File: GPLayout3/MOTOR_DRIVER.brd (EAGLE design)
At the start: 129.7 x 96.6 mm, 95 parts, among them T1 2N2222, T2 2N2222, U7 ATMEGA328P_TQFP, Y1 16MHz

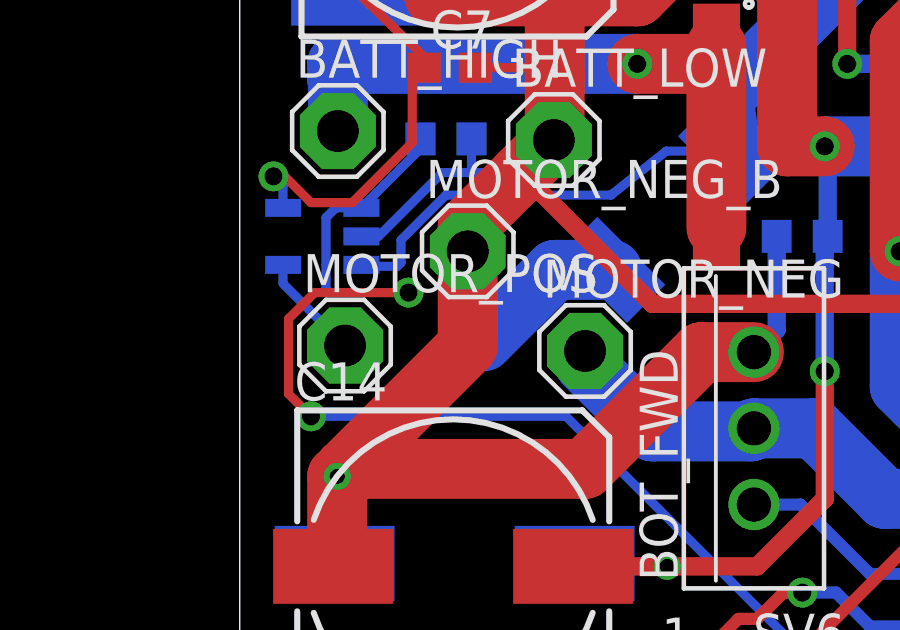
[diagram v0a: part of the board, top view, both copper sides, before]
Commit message: Fixed missing wire
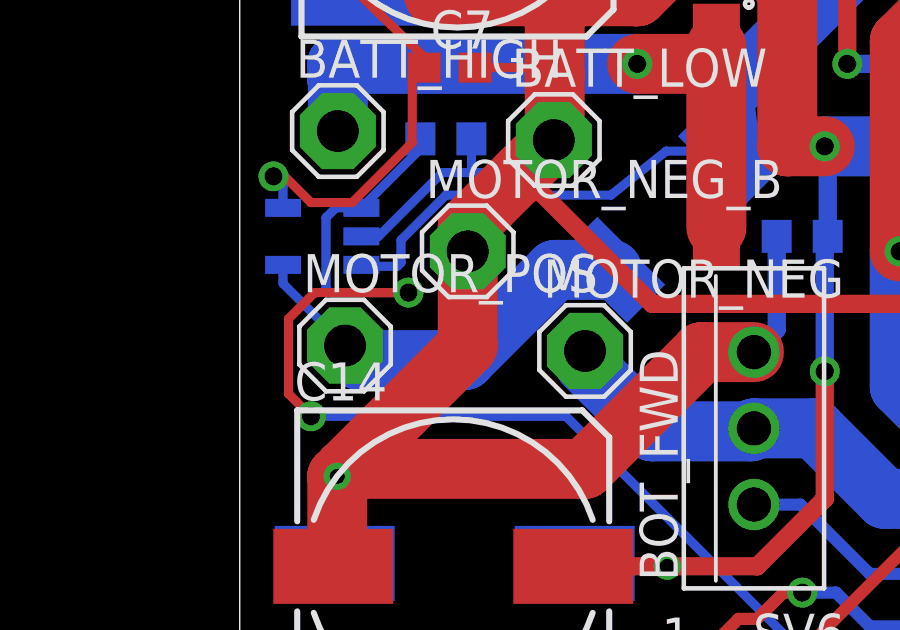
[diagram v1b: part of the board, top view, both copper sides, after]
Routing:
- net I_SENSE_LOW_TOP: track 9.02 -> 14.1 mm
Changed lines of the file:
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@@
 <wire x1="12.41464375" y1="67.38185" x2="10.50685" y2="67.38185" width="2" layer="16"/>
 <wire x1="3.51" y1="64.86" x2="3.65" y2="65" width="2" layer="16"/>
-<wire x1="10.50685" y1="67.38185" x2="8.125" y2="65" width="2" layer="16"/>
 <wire x1="1.444" y1="67.55" x2="1.444" y2="66.926" width="0.3048" layer="16"/>
 <wire x1="1.444" y1="66.926" x2="3.51" y2="64.86" width="0.3048" layer="16"/>
-<wire x1="3.65" y1="65" x2="8.125" y2="65" width="0" layer="19" extent="16-16"/>
+<wire x1="7.5" y1="64.375" x2="3.995" y2="64.375" width="2" layer="16"/>
+<wire x1="3.995" y1="64.375" x2="3.51" y2="64.86" width="2" layer="16"/>
+<wire x1="10.50685" y1="67.38185" x2="7.5" y2="64.375" width="2" layer="16"/>
 </signal>
 <signal name="I_SENSE_HI">

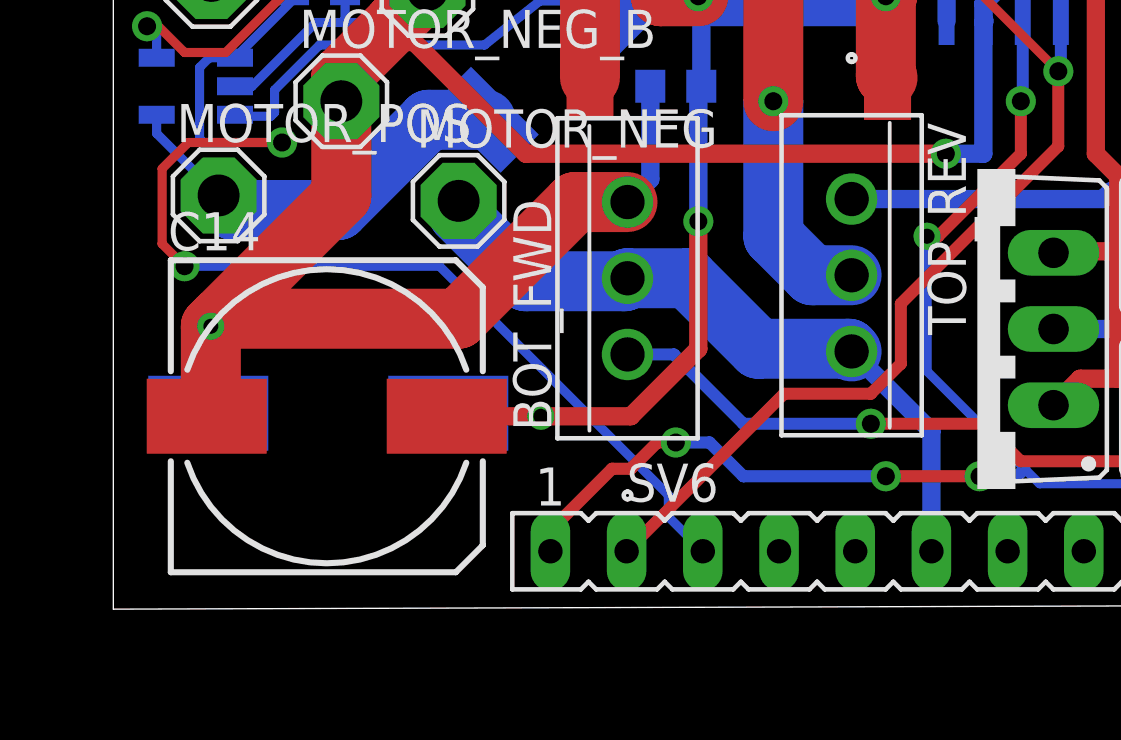
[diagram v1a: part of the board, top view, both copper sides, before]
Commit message: Fixed missing motor_high_top pin, now I_SENSE_LOW_TOP
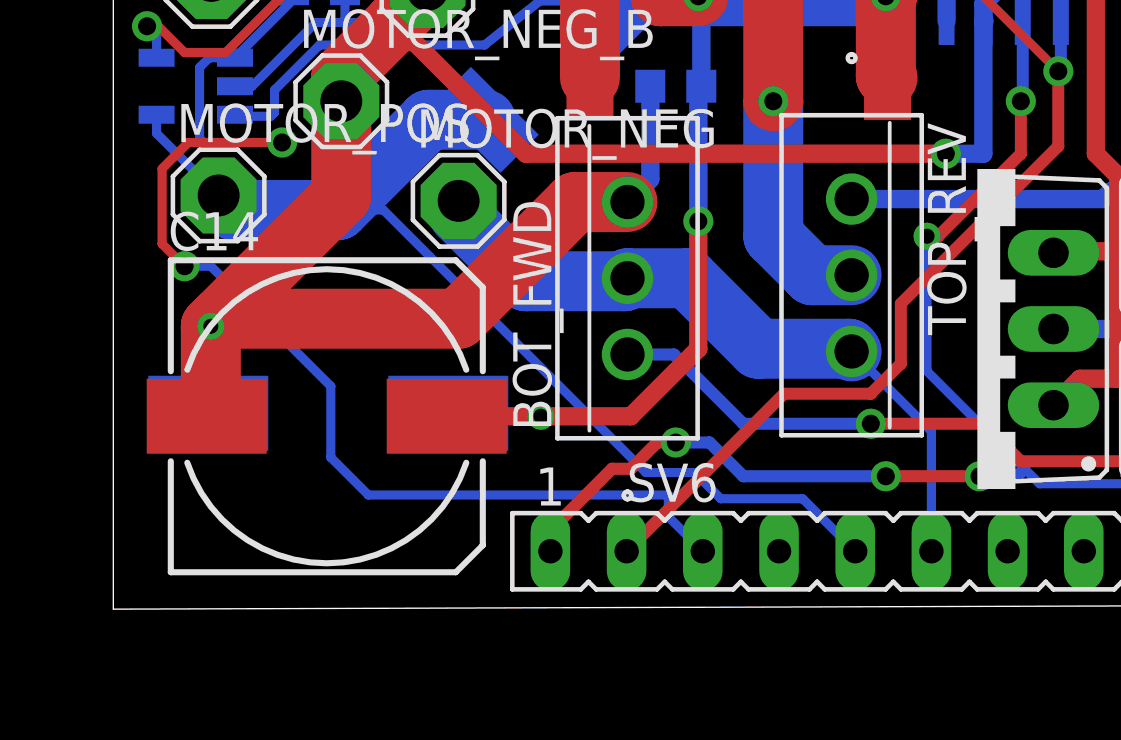
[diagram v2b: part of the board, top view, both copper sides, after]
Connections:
- removed net MOTOR_HIGH_TOP: SV6.5
- net I_SENSE_LOW_TOP: now also SV6.5
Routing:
- net I_SENSE_LOW_TOP: track 14.1 -> 36.0 mm
- net I_SENSE_TOP: track 39.2 -> 40.6 mm
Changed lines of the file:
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@@
 <wire x1="18.51" y1="23.49" x2="22.49" y2="23.554" width="0" layer="19" extent="1-1"/>
-</signal>
-<signal name="MOTOR_HIGH_TOP">
-<contactref element="SV6" pad="5"/>
 </signal>
 <signal name="MOTOR_LOW_TOP">
@@
 <wire x1="21.5" y1="59.75" x2="24.52" y2="59.75" width="2" layer="16"/>
 <wire x1="24.61" y1="59.66" x2="24.52" y2="59.75" width="2" layer="16"/>
-<wire x1="27.27" y1="53" x2="27.27" y2="57" width="0.6096" layer="16"/>
-<wire x1="27.27" y1="57" x2="24.61" y2="59.66" width="0.6096" layer="16"/>
+<wire x1="27.27" y1="53" x2="27.27" y2="57" width="0.3048" layer="16"/>
+<wire x1="27.27" y1="57" x2="24.61" y2="59.66" width="0.3048" layer="16"/>
 </signal>
 <signal name="HI2">
@@
 <wire x1="1.444" y1="67.55" x2="1.444" y2="66.926" width="0.3048" layer="16"/>
 <wire x1="1.444" y1="66.926" x2="3.51" y2="64.86" width="0.3048" layer="16"/>
-<wire x1="7.5" y1="64.375" x2="3.995" y2="64.375" width="2" layer="16"/>
+<wire x1="3.995" y1="64.375" x2="7.5" y2="64.375" width="2" layer="16"/>
 <wire x1="3.995" y1="64.375" x2="3.51" y2="64.86" width="2" layer="16"/>
 <wire x1="10.50685" y1="67.38185" x2="7.5" y2="64.375" width="2" layer="16"/>
+<contactref element="SV6" pad="5"/>
+<wire x1="7.5" y1="64.375" x2="9" y2="64.375" width="0.3048" layer="16"/>
+<wire x1="17.75" y1="55.625" x2="19.375" y2="55.625" width="0.3048" layer="16"/>
+<wire x1="20.25" y1="54.75" x2="22.98" y2="54.75" width="0.3048" layer="16"/>
+<wire x1="22.98" y1="54.75" x2="24.73" y2="53" width="0.3048" layer="16"/>
+<wire x1="9" y1="64.375" x2="17.75" y2="55.625" width="0.3048" layer="16"/>
+<wire x1="19.375" y1="55.625" x2="20.25" y2="54.75" width="0.3048" layer="16"/>
 </signal>
 <signal name="I_SENSE_HI">
@@
 <wire x1="1.625" y1="63.25" x2="2.375" y2="62.5" width="0.3048" layer="1"/>
 <via x="2.375" y="62.5" extent="1-16" drill="0.6" shape="square"/>
-<wire x1="2.375" y1="62.5" x2="10.875" y2="62.5" width="0.3048" layer="16"/>
-<wire x1="10.875" y1="62.5" x2="18.5" y2="54.875" width="0.3048" layer="16"/>
-<wire x1="18.5" y1="54.875" x2="18.5" y2="54.15" width="0.3048" layer="16"/>
+<wire x1="18.5" y1="54.15" x2="18.5" y2="54.875" width="0.3048" layer="16"/>
 <wire x1="18.5" y1="54.15" x2="19.65" y2="53" width="0.3048" layer="16"/>
+<wire x1="18.5" y1="54.875" x2="8.5" y2="54.875" width="0.3048" layer="16"/>
+<wire x1="8.5" y1="54.875" x2="7.25" y2="56.125" width="0.3048" layer="16"/>
+<wire x1="7.25" y1="56.125" x2="7.25" y2="58.5" width="0.3048" layer="16"/>
+<wire x1="3.25" y1="62.5" x2="2.375" y2="62.5" width="0.3048" layer="16"/>
+<wire x1="7.25" y1="58.5" x2="3.25" y2="62.5" width="0.3048" layer="16"/>
 </signal>
 </signals>

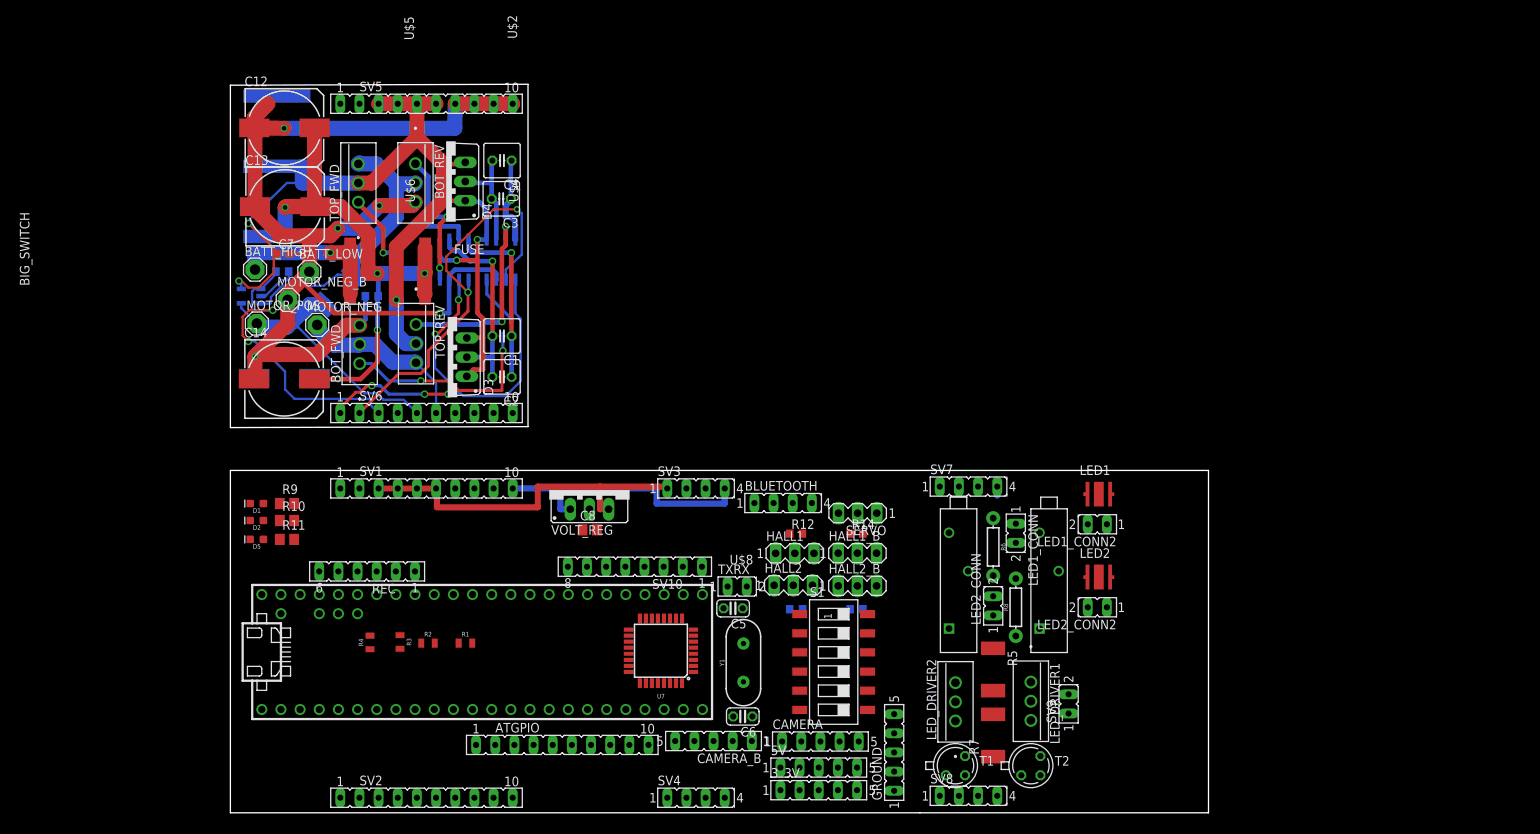
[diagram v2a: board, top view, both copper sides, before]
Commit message: Routed lower board and combined all boards
typical_4pcb.dru lists design errors for the width of the traces, but
the file is outdated and trace widths correspond with 4pcb's website
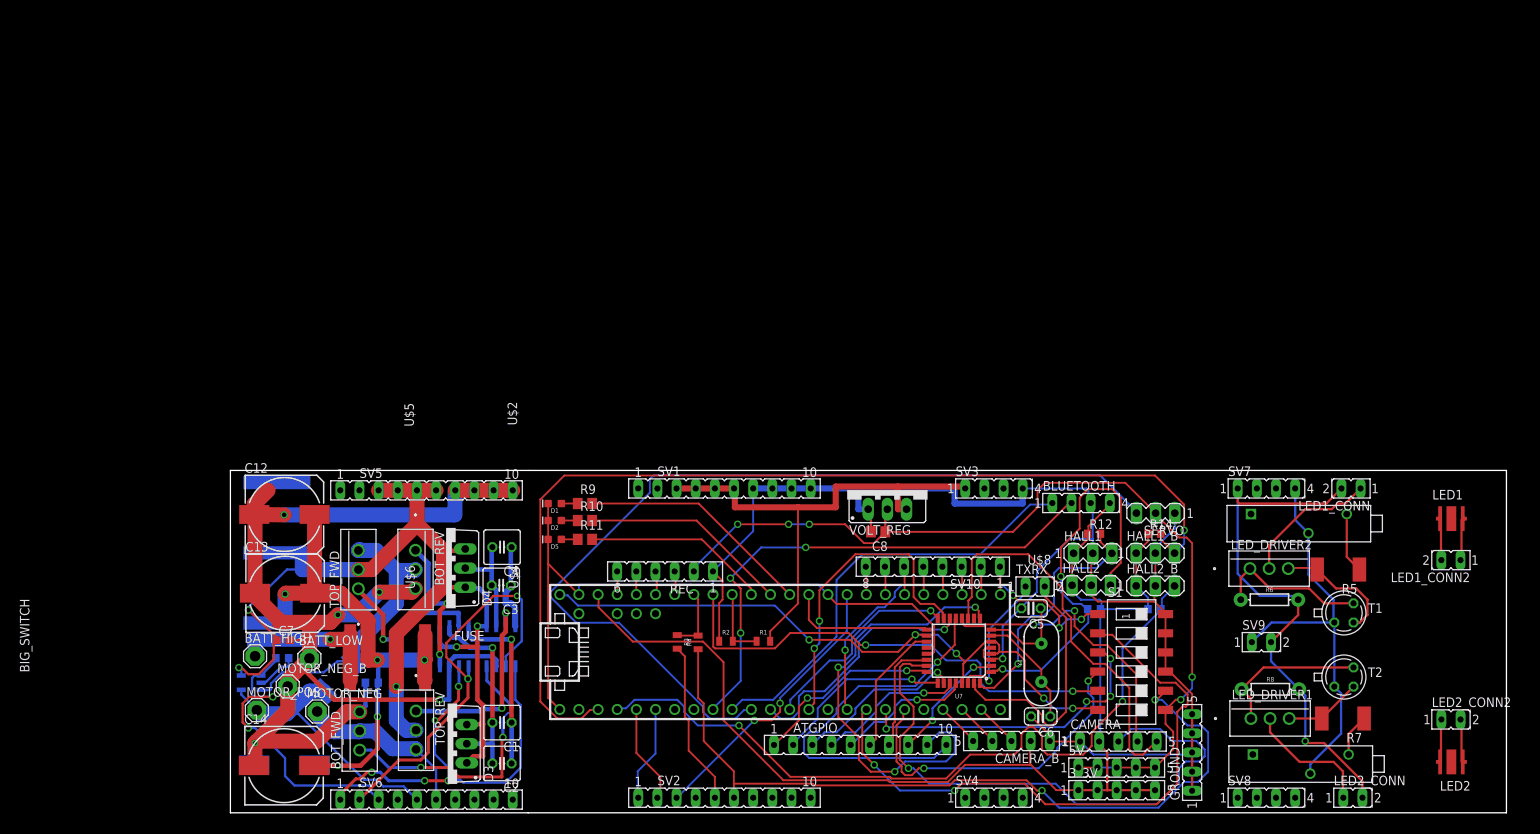
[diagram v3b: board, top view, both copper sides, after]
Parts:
- moved LED2_CONN 59.2 mm to (152.6, 2.00), turned to 0 degrees
- moved LED2_CONN2 56.5 mm to (165.6, 12.4), turned to 0 degrees
- moved T1 55.3 mm to (147.6, 26.5)
- moved LED2 52.8 mm to (161.9, 6.75), turned to 180 degrees
- moved C3 51.3 mm to (35.9, 30.1)
- moved MOTOR_NEG 51.3 mm to (11.5, 13.4)
- moved BATT_HIGH 51.2 mm to (3.27, 20.8)
- moved BIG_SWITCH 51.2 mm to (6.16, 29.8)
- moved BOT_FWD 51.2 mm to (17.1, 13.4)
- moved BOT_REV 51.2 mm to (24.5, 29.7)
- moved C1 51.2 mm to (36.0, 12.0)
- moved C12 51.2 mm to (7.17, 39.5)
- moved C13 51.2 mm to (7.26, 29.1)
- moved C14 51.2 mm to (7.12, 6.25)
- moved C15 51.2 mm to (7.17, 6.35)
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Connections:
- removed net I_SENSE_HI: SV1.2
- removed net I_SENSE_LOW: SV1.1
- net HI2: no longer SV2.3
- net I_SENSE: now also SV2.3
- net LI2: no longer SV2.4
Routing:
- net GND: track 36.2 -> 284.5 mm, vias 0 -> 1
- net 3_3V: track 0.00 -> 156.5 mm
- net HALL1_B: track 0.00 -> 134.5 mm, vias 0 -> 1
- net 5V: track 0.00 -> 124.3 mm, vias 0 -> 5
- net SERVO: track 0.00 -> 122.2 mm
- net MOTOR_LOW: track 0.00 -> 104.3 mm, vias 0 -> 2
- net HALL2_B: track 0.00 -> 101.0 mm, vias 0 -> 2
- net 5V_TEENSY: track 0.00 -> 89.5 mm, vias 0 -> 5
- net SW2: track 0.00 -> 80.4 mm, vias 0 -> 2
- net CAMERA_A0: track 0.00 -> 78.3 mm, vias 0 -> 1
- net 7_4V_TOP2: track 0.00 -> 71.3 mm, vias 0 -> 1
- net BLT_TX: track 0.00 -> 68.9 mm, vias 0 -> 3
- net EMF_SENSE_LOW: track 0.00 -> 63.5 mm, vias 0 -> 2
- net PD5: track 0.00 -> 58.9 mm, vias 0 -> 3
- net BLT_RX: track 0.00 -> 58.3 mm
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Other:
- board size 129.7 x 96.6 mm -> 169.2 x 45.4 mm
